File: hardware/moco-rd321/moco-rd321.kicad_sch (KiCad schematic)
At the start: 33 parts, among them J1 I^{2}C, J2 Serial, J3 Debug, J4 V+, J5 V-, SW1 RESET, U1 STSPIN32F0A

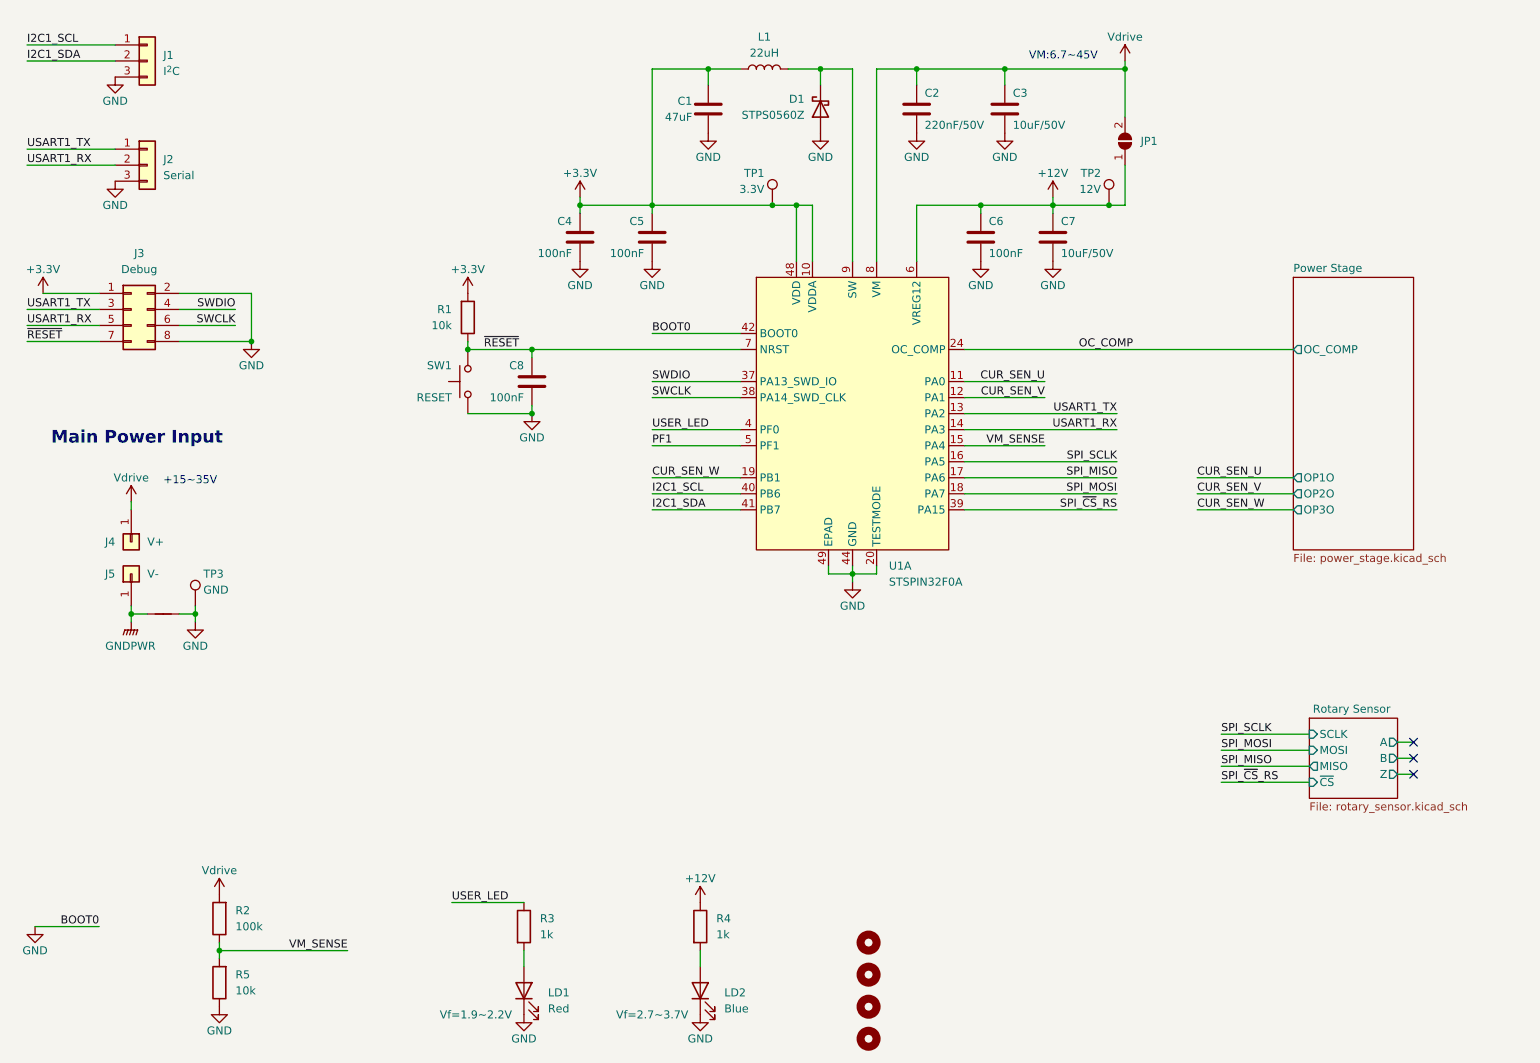
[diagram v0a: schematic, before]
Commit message: Rename RD401 to RD321
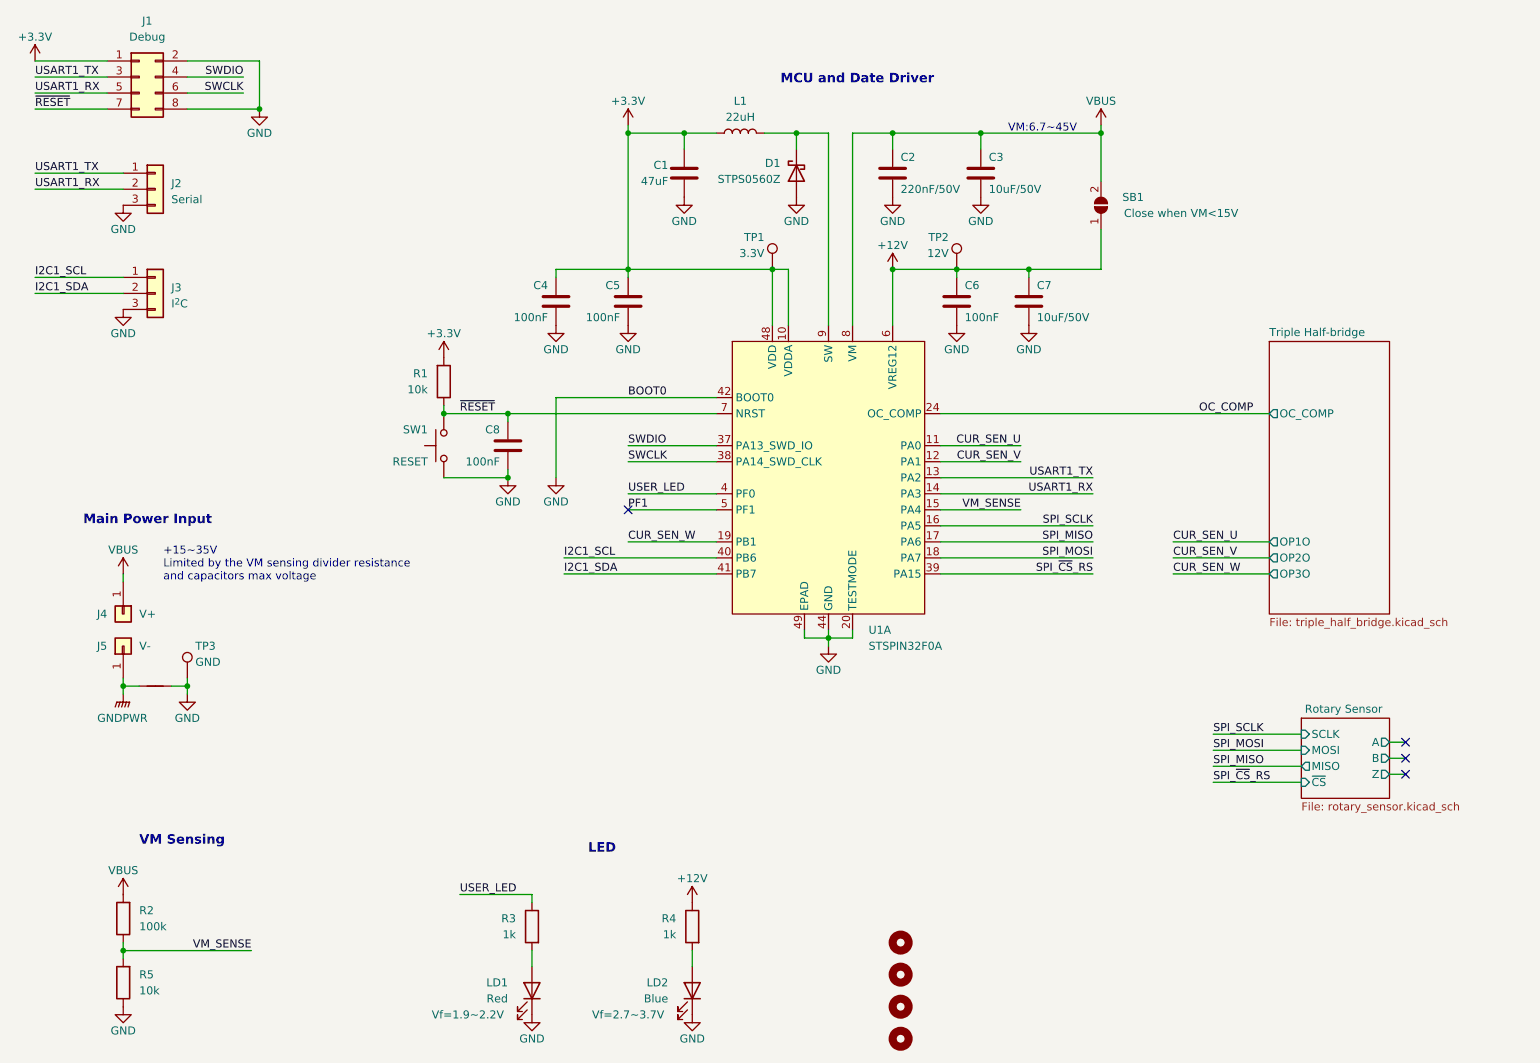
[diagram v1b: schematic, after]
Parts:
- J4: footprint moco:wire_2.2mm -> moco:wire_2.2mm_rectagnel
- SB1: renamed from JP1; Note (none) -> Close when VM<15V
- renumbered J3 to J1, J1 to J3
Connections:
- net Vdrive renamed VBUS
- no-connect marks 3 -> 4
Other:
- sheet Power Stage renamed Triple Half-bridge
- sheet Triple Half-bridge: file power_stage.kicad_sch -> triple_half_bridge.kicad_sch
- note added: "+15~35V Limited by the VM sensing divider resistance and capacitors max voltage"
- note added: "LED"
- note added: "MCU and Date Driver"
- note added: "VM Sensing"
- note removed: "+15~35V"
- title: (none) -> moco-RD321
- moved on the sheet: C1, C2, C3, C4, C5, C6, C7, C8, D1, J1, J2, J3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

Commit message: Update readme
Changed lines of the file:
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@@
+    (stroke (width 0) (type default))
+  )
+  (wire (pts (xy 57.15 134.62) (xy 57.15 133.35))
+    (stroke (width 0) (type default))
+  )
+  (wire (pts (xy 190.5 68.58) (xy 190.5 67.31))
+    (stroke (width 0) (type default))
+  )
+  (wire (pts (xy 176.53 102.87) (xy 200.66 102.87))
+    (stroke (width 0) (type default))
+  )
+  (wire (pts (xy 33.02 52.07) (xy 46.99 52.07))
+    (stroke (width 0) (type default))
+  )
+  (wire (pts (xy 54.61 133.35) (xy 57.15 133.35))
+    (stroke (width 0) (type default))
+  )
+  (wire (pts (xy 189.23 97.79) (xy 176.53 97.79))
+    (stroke (width 0) (type default))
+  )
+  (wire (pts (xy 162.56 45.72) (xy 162.56 76.2))
+    (stroke (width 0) (type default))
+  )
+  (wire (pts (xy 153.67 45.72) (xy 158.75 45.72))
+    (stroke (width 0) (type default))
+  )
+  (wire (pts (xy 127 67.31) (xy 127 68.58))
+    (stroke (width 0) (type default))
+  )
+  (wire (pts (xy 127 110.49) (xy 140.97 110.49))
+    (stroke (width 0) (type default))
+  )
+  (wire (pts (xy 219.71 140.97) (xy 233.68 140.97))
+    (stroke (width 0) (type default))
+  )
+  (wire (pts (xy 168.91 45.72) (xy 162.56 45.72))
+    (stroke (width 0) (type default))
+  )
+  (wire (pts (xy 66.04 36.83) (xy 57.15 36.83))
+    (stroke (width 0) (type default))
+  )
+  (wire (pts (xy 116.84 115.57) (xy 140.97 115.57))
+    (stroke (width 0) (type default))
+  )
+  (wire (pts (xy 247.65 147.32) (xy 250.19 147.32))
+    (stroke (width 0) (type default))
+  )
+  (wire (pts (xy 57.15 34.29) (xy 68.58 34.29))
+    (stroke (width 0) (type default))
+  )
+  (wire (pts (xy 149.86 67.31) (xy 149.86 76.2))
+    (stroke (width 0) (type default))
+  )
+  (wire (pts (xy 219.71 146.05) (xy 233.68 146.05))
+    (stroke (width 0) (type default))
+  )
+  (wire (pts (xy 162.56 125.73) (xy 158.75 125.73))
+    (stroke (width 0) (type default))
+  )
+  (wire (pts (xy 97.79 100.33) (xy 107.95 100.33))
+    (stroke (width 0) (type default))
+  )
+  (wire (pts (xy 49.53 133.35) (xy 46.99 133.35))
+    (stroke (width 0) (type default))
+  )
+  (wire (pts (xy 189.23 95.25) (xy 176.53 95.25))
+    (stroke (width 0) (type default))
+  )
+  (wire (pts (xy 46.99 134.62) (xy 46.99 133.35))
+    (stroke (width 0) (type default))
+  )
+  (wire (pts (xy 213.36 113.03) (xy 228.6 113.03))
+    (stroke (width 0) (type default))
+  )
+  (wire (pts (xy 127 102.87) (xy 140.97 102.87))
+    (stroke (width 0) (type default))
+  )
+  (wire (pts (xy 176.53 115.57) (xy 200.66 115.57))
+    (stroke (width 0) (type default))
+  )
+  (wire (pts (xy 182.88 48.26) (xy 182.88 45.72))
+    (stroke (width 0) (type default))
+  )
+  (wire (pts (xy 33.02 39.37) (xy 44.45 39.37))
+    (stroke (width 0) (type default))
+  )
+  (wire (pts (xy 68.58 34.29) (xy 68.58 41.91))
+    (stroke (width 0) (type default))
+  )
+  (wire (pts (xy 111.76 166.37) (xy 111.76 167.64))
+    (stroke (width 0) (type default))
+  )
+  (wire (pts (xy 149.86 67.31) (xy 152.4 67.31))
+    (stroke (width 0) (type default))
+  )
+  (wire (pts (xy 176.53 100.33) (xy 200.66 100.33))
+    (stroke (width 0) (type default))
+  )
+  (wire (pts (xy 100.33 166.37) (xy 111.76 166.37))
+    (stroke (width 0) (type default))
+  )
+  (wire (pts (xy 213.36 115.57) (xy 228.6 115.57))
+    (stroke (width 0) (type default))
+  )
+  (wire (pts (xy 176.53 113.03) (xy 200.66 113.03))
+    (stroke (width 0) (type default))
+  )
+  (wire (pts (xy 33.02 54.61) (xy 46.99 54.61))
+    (stroke (width 0) (type default))
+  )
+  (wire (pts (xy 33.02 68.58) (xy 46.99 68.58))
+    (stroke (width 0) (type default))
+  )
+  (wire (pts (xy 127 45.72) (xy 135.89 45.72))
+    (stroke (width 0) (type default))
+  )
+  (wire (pts (xy 247.65 144.78) (xy 250.19 144.78))
+    (stroke (width 0) (type default))
+  )
+  (wire (pts (xy 135.89 45.72) (xy 135.89 48.26))
+    (stroke (width 0) (type default))
+  )
+  (wire (pts (xy 46.99 173.99) (xy 46.99 175.26))
+    (stroke (width 0) (type default))
+  )
+  (wire (pts (xy 33.02 71.12) (xy 46.99 71.12))
+    (stroke (width 0) (type default))
+  )
+  (wire (pts (xy 152.4 76.2) (xy 152.4 67.31))
+    (stroke (width 0) (type default))
+  )
+  (wire (pts (xy 219.71 148.59) (xy 233.68 148.59))
+    (stroke (width 0) (type default))
+  )
+  (wire (pts (xy 97.79 90.17) (xy 107.95 90.17))
     (stroke (width 0) (type default))
   )
@@
     (stroke (width 0) (type default))
   )
-  (wire (pts (xy 57.15 134.62) (xy 57.15 133.35))
-    (stroke (width 0) (type default))
-  )
-  (wire (pts (xy 190.5 68.58) (xy 190.5 67.31))
-    (stroke (width 0) (type default))
-  )
-  (wire (pts (xy 176.53 102.87) (xy 200.66 102.87))
-    (stroke (width 0) (type default))
-  )
-  (wire (pts (xy 33.02 52.07) (xy 46.99 52.07))
-    (stroke (width 0) (type default))
-  )
-  (wire (pts (xy 54.61 133.35) (xy 57.15 133.35))
-    (stroke (width 0) (type default))
-  )
-  (wire (pts (xy 189.23 97.79) (xy 176.53 97.79))
-    (stroke (width 0) (type default))
-  )
-  (wire (pts (xy 162.56 45.72) (xy 162.56 76.2))
-    (stroke (width 0) (type default))
-  )
-  (wire (pts (xy 153.67 45.72) (xy 158.75 45.72))
-    (stroke (width 0) (type default))
-  )
-  (wire (pts (xy 127 67.31) (xy 127 68.58))
-    (stroke (width 0) (type default))
-  )
-  (wire (pts (xy 127 110.49) (xy 140.97 110.49))
-    (stroke (width 0) (type default))
-  )
-  (wire (pts (xy 219.71 140.97) (xy 233.68 140.97))
-    (stroke (width 0) (type default))
-  )
-  (wire (pts (xy 168.91 45.72) (xy 162.56 45.72))
-    (stroke (width 0) (type default))
-  )
-  (wire (pts (xy 66.04 36.83) (xy 57.15 36.83))
-    (stroke (width 0) (type default))
-  )
-  (wire (pts (xy 116.84 115.57) (xy 140.97 115.57))
-    (stroke (width 0) (type default))
-  )
-  (wire (pts (xy 247.65 147.32) (xy 250.19 147.32))
-    (stroke (width 0) (type default))
-  )
-  (wire (pts (xy 57.15 34.29) (xy 68.58 34.29))
-    (stroke (width 0) (type default))
-  )
-  (wire (pts (xy 149.86 67.31) (xy 149.86 76.2))
-    (stroke (width 0) (type default))
-  )
-  (wire (pts (xy 219.71 146.05) (xy 233.68 146.05))
-    (stroke (width 0) (type default))
-  )
-  (wire (pts (xy 162.56 125.73) (xy 158.75 125.73))
-    (stroke (width 0) (type default))
-  )
-  (wire (pts (xy 97.79 100.33) (xy 107.95 100.33))
-    (stroke (width 0) (type default))
-  )
-  (wire (pts (xy 49.53 133.35) (xy 46.99 133.35))
-    (stroke (width 0) (type default))
-  )
-  (wire (pts (xy 189.23 95.25) (xy 176.53 95.25))
-    (stroke (width 0) (type default))
-  )
-  (wire (pts (xy 46.99 134.62) (xy 46.99 133.35))
-    (stroke (width 0) (type default))
-  )
-  (wire (pts (xy 127 102.87) (xy 140.97 102.87))
-    (stroke (width 0) (type default))
-  )
-  (wire (pts (xy 176.53 115.57) (xy 200.66 115.57))
-    (stroke (width 0) (type default))
-  )
-  (wire (pts (xy 182.88 48.26) (xy 182.88 45.72))
-    (stroke (width 0) (type default))
-  )
-  (wire (pts (xy 33.02 39.37) (xy 44.45 39.37))
-    (stroke (width 0) (type default))
-  )
-  (wire (pts (xy 68.58 34.29) (xy 68.58 41.91))
-    (stroke (width 0) (type default))
-  )
-  (wire (pts (xy 111.76 166.37) (xy 111.76 167.64))
-    (stroke (width 0) (type default))
-  )
-  (wire (pts (xy 149.86 67.31) (xy 152.4 67.31))
-    (stroke (width 0) (type default))
-  )
-  (wire (pts (xy 176.53 100.33) (xy 200.66 100.33))
-    (stroke (width 0) (type default))
-  )
-  (wire (pts (xy 100.33 166.37) (xy 111.76 166.37))
-    (stroke (width 0) (type default))
-  )
-  (wire (pts (xy 176.53 113.03) (xy 200.66 113.03))
-    (stroke (width 0) (type default))
-  )
-  (wire (pts (xy 33.02 54.61) (xy 46.99 54.61))
-    (stroke (width 0) (type default))
-  )
-  (wire (pts (xy 33.02 68.58) (xy 46.99 68.58))
-    (stroke (width 0) (type default))
-  )
-  (wire (pts (xy 127 45.72) (xy 135.89 45.72))
-    (stroke (width 0) (type default))
-  )
-  (wire (pts (xy 247.65 144.78) (xy 250.19 144.78))
-    (stroke (width 0) (type default))
-  )
-  (wire (pts (xy 135.89 45.72) (xy 135.89 48.26))
-    (stroke (width 0) (type default))
-  )
-  (wire (pts (xy 46.99 173.99) (xy 46.99 175.26))
-    (stroke (width 0) (type default))
-  )
-  (wire (pts (xy 33.02 71.12) (xy 46.99 71.12))
-    (stroke (width 0) (type default))
-  )
-  (wire (pts (xy 152.4 76.2) (xy 152.4 67.31))
-    (stroke (width 0) (type default))
-  )
-  (wire (pts (xy 219.71 148.59) (xy 233.68 148.59))
-    (stroke (width 0) (type default))
-  )
-  (wire (pts (xy 97.79 90.17) (xy 107.95 90.17))
-    (stroke (width 0) (type default))
-  )
   (wire (pts (xy 158.75 125.73) (xy 158.75 127))
     (stroke (width 0) (type default))
@@
     (stroke (width 0) (type default))
   )
-  (wire (pts (xy 213.36 115.57) (xy 228.6 115.57))
-    (stroke (width 0) (type default))
-  )
   (wire (pts (xy 176.53 110.49) (xy 200.66 110.49))
     (stroke (width 0) (type default))
   )
   (wire (pts (xy 190.5 67.31) (xy 201.93 67.31))
-    (stroke (width 0) (type default))
-  )
-  (wire (pts (xy 213.36 113.03) (xy 228.6 113.03))
     (stroke (width 0) (type default))
   )
@@
     (effects (font (size 1.27 1.27)) (justify right bottom))
   )
-  (label "CUR_SEN_U" (at 213.36 110.49 0) (fields_autoplaced)
+  (label "CUR_SEN_U" (at 213.36 115.57 0) (fields_autoplaced)
     (effects (font (size 1.27 1.27)) (justify left bottom))
   )
@@
     (effects (font (size 1.27 1.27)) (justify right bottom))
   )
-  (label "CUR_SEN_W" (at 213.36 115.57 0) (fields_autoplaced)
-    (effects (font (size 1.27 1.27)) (justify left bottom))
-  )
+  (label "CUR_SEN_W" (at 213.36 110.49 0) (fields_autoplaced)
+    (effects (font (size 1.27 1.27)) (justify left bottom))
+  )
